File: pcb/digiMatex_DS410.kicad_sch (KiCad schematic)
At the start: 37 parts, among them J1 POWER, J2 E, J3 A/B, J4 Buttons, Q1 PN2222A, Q2 PN2222A, Q3 PN2222A, U1 MAX7219, U2 L7805

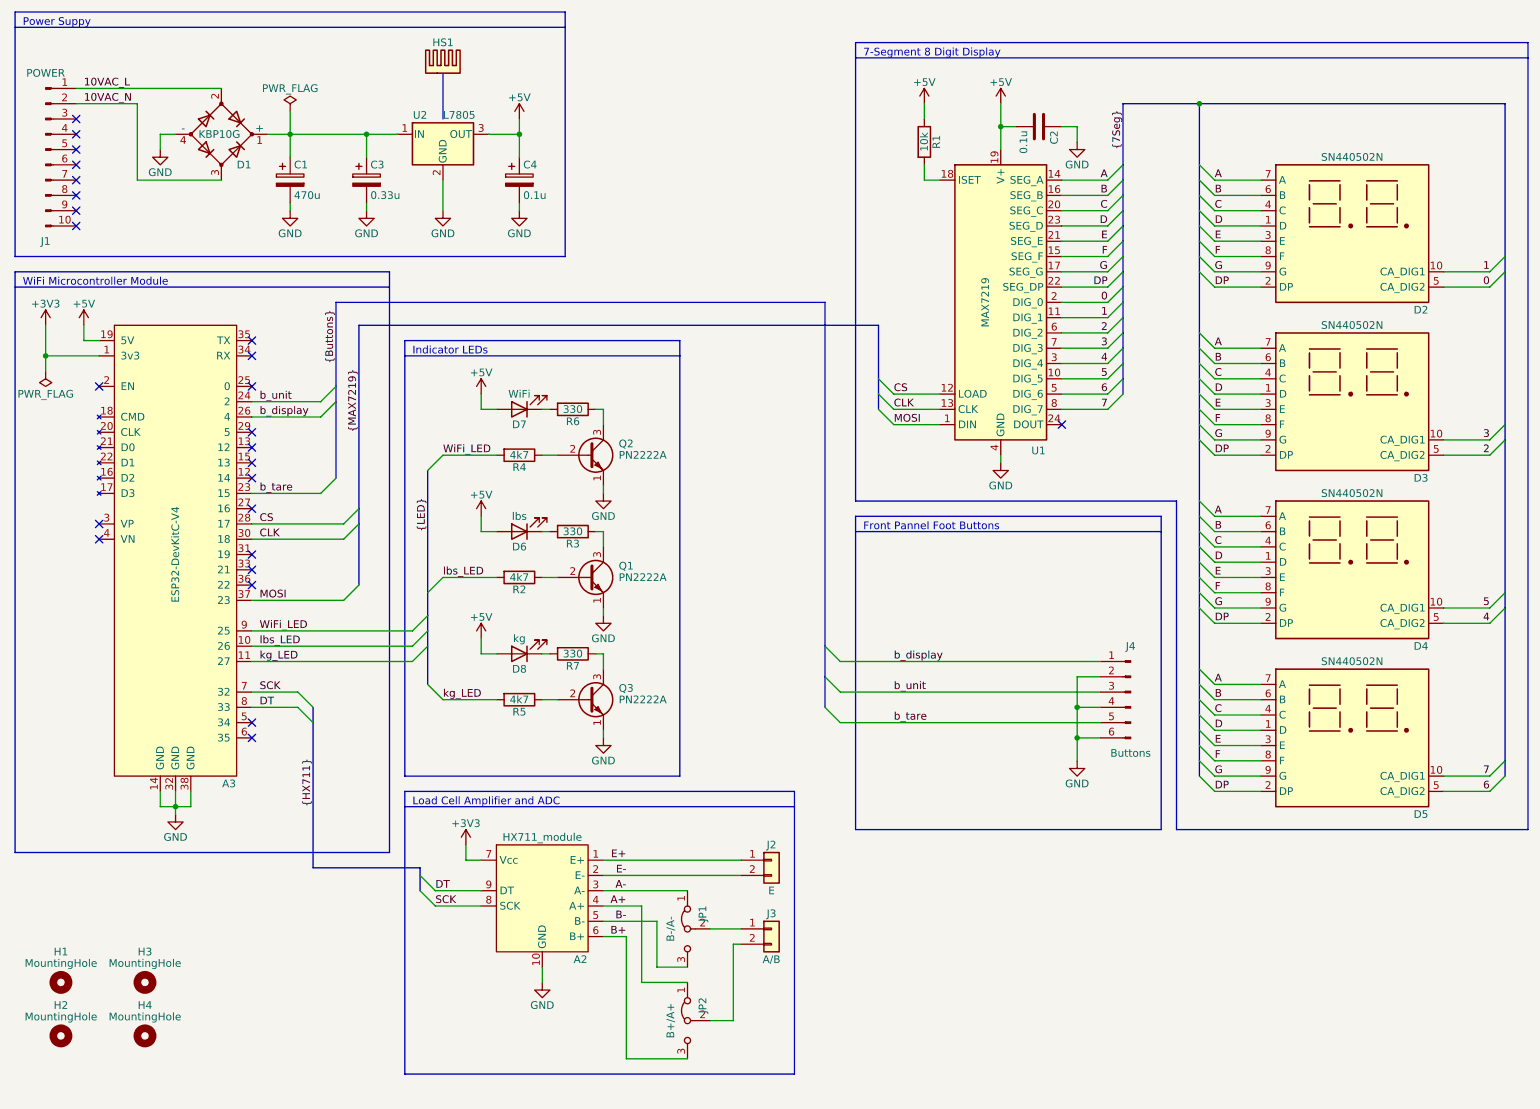
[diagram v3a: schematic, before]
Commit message: rev A schematic with more SMD
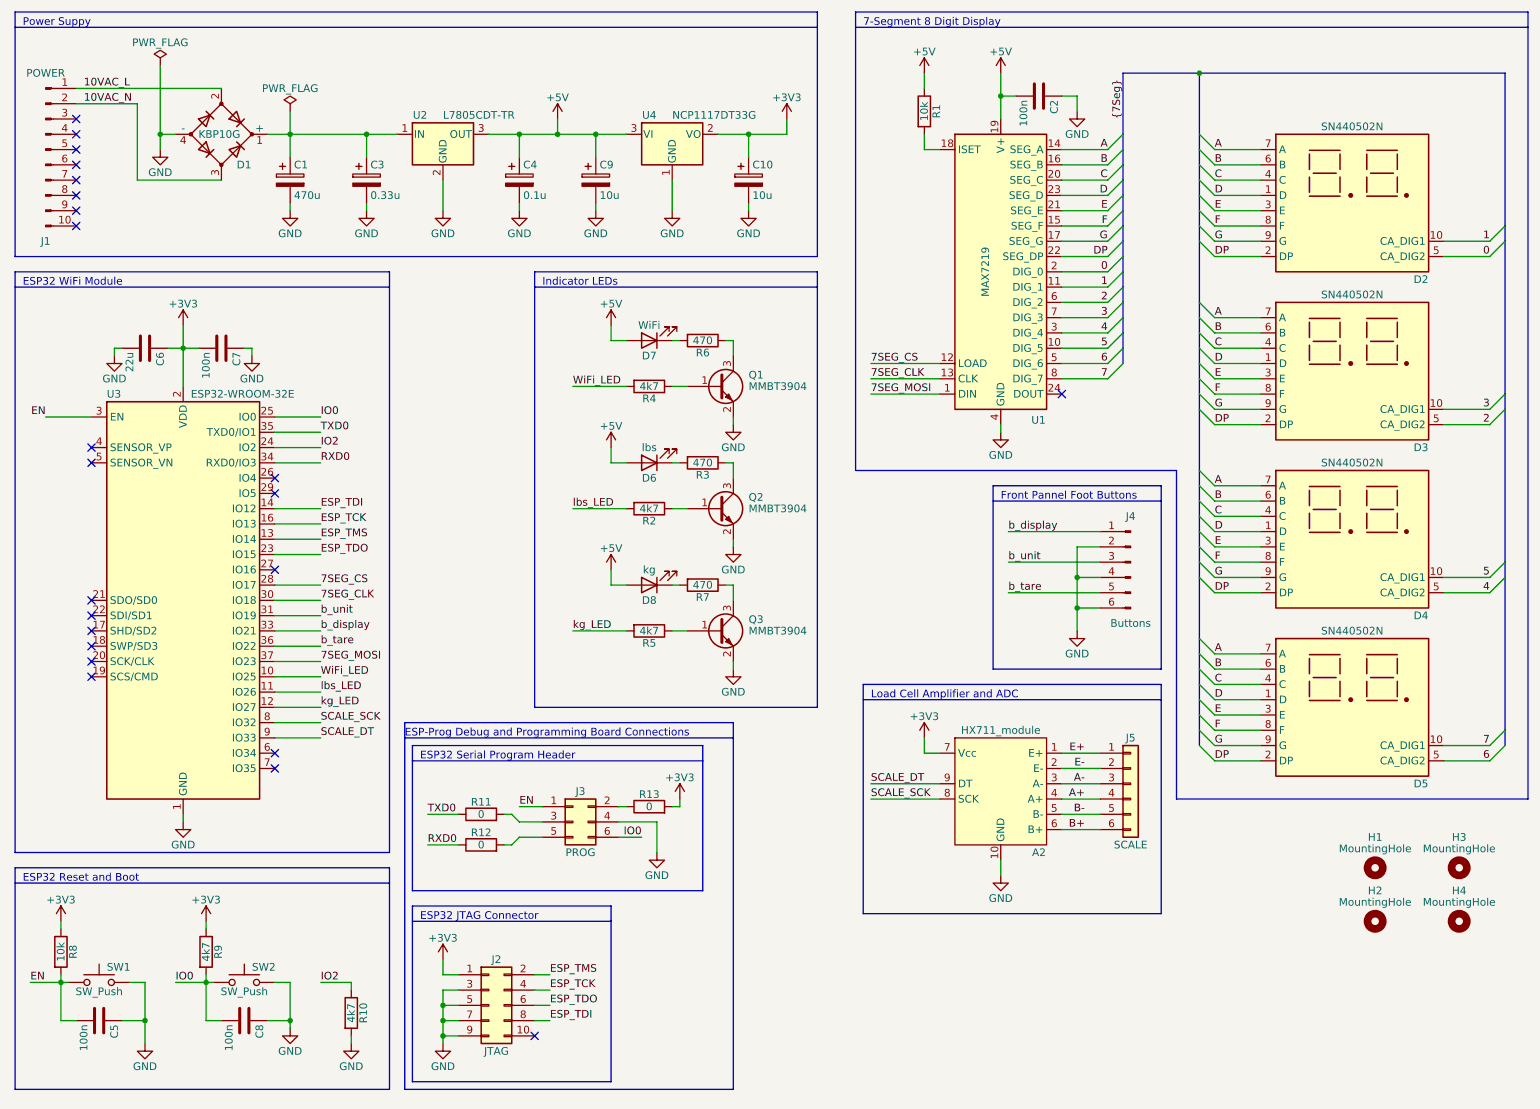
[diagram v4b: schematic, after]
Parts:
- removed A3: ESP32-DevKitC-V4, pl_esp:esp32_devkitc_v4, symbol pl_esp32:ESP32-DevKitC-V4
- removed HS1: Heatsink, pl_heatsink:TO-220hs_16x16x25mm_2pins, symbol Mechanical:Heatsink
- removed J2: E, pl_TerminalBlock:WJ127-5.0-2P, symbol Connector_Generic:Conn_01x02
- removed J3: A/B, pl_TerminalBlock:WJ127-5.0-2P, symbol Connector_Generic:Conn_01x02
- removed JP1: B-/A-, Connector_PinHeader_2.54mm:PinHeader_1x03_P2.54mm_Vertical, symbol Jumper:Jumper_3_Bridged12
- removed JP2: B+/A+, Connector_PinHeader_2.54mm:PinHeader_1x03_P2.54mm_Vertical, symbol Jumper:Jumper_3_Bridged12
- removed Q1, Q2, Q3: PN2222A, Package_TO_SOT_THT:TO-92_Inline, symbol Transistor_BJT:PN2222A
- added C10, C9: 10u, Capacitor_THT:CP_Radial_D6.3mm_P2.50mm, symbol Device:C_Polarized
- added C5, C7, C8: 100n, Capacitor_SMD:C_0603_1608Metric, symbol Device:C
- added C6: 22u, Capacitor_SMD:C_1206_3216Metric, symbol Device:C
- added J2: JTAG, Connector_PinHeader_2.54mm:PinHeader_2x05_P2.54mm_Vertical, symbol Connector_Generic:Conn_02x05_Odd_Even
- added J3: PROG, Connector_PinHeader_2.54mm:PinHeader_2x03_P2.54mm_Vertical, symbol Connector_Generic:Conn_02x03_Odd_Even
- added J5: SCALE, TerminalBlock_Phoenix:TerminalBlock_Phoenix_MKDS-1,5-6_1x06_P5.00mm_Horizontal, symbol Connector_Generic:Conn_01x06
- added Q1, Q2, Q3: MMBT3904, Package_TO_SOT_SMD:SOT-23, symbol Transistor_BJT:MMBT3904
- added R10, R9: 4k7, Capacitor_SMD:C_0603_1608Metric, symbol Device:R
- added R11, R12, R13: 0, Capacitor_SMD:C_0805_2012Metric, symbol Device:R
- added R8: 10k, Capacitor_SMD:C_0603_1608Metric, symbol Device:R
- added SW1, SW2: SW_Push, Button_Switch_THT:SW_PUSH_6mm, symbol Switch:SW_Push
- added U3: ESP32-WROOM-32E, RF_Module:ESP32-WROOM-32, symbol RF_Module:ESP32-WROOM-32D
- added U4: NCP1117DT33G, Package_TO_SOT_SMD:TO-252-2, symbol Regulator_Linear:NCP1117-3.3_TO252
- C2: value 0.1u -> 100n; footprint Capacitor_THT:C_Disc_D4.3mm_W1.9mm_P5.00mm -> Capacitor_SMD:C_0603_1608Metric
- R1, R2, R4, R5: footprint Resistor_THT:R_Axial_DIN0207_L6.3mm_D2.5mm_P15.24mm_Horizontal -> Capacitor_SMD:C_0603_1608Metric
- R3, R6, R7: value 330 -> 470; footprint Resistor_THT:R_Axial_DIN0207_L6.3mm_D2.5mm_P15.24mm_Horizontal -> Capacitor_SMD:C_0805_2012Metric
- U2: value L7805 -> L7805CDT-TR; footprint Package_TO_SOT_THT:TO-220-3_Vertical -> Package_TO_SOT_SMD:TO-252-2
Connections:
- net +3V3: now also C10.1, C6.1, C7.2, J2.1 (Pin_1), R13.2, R8.1, R9.1, U3.2 (VDD), U4.2 (VO)
- net +5V: now also C9.1, U4.3 (VI)
- net A+: now also J5.4 (Pin_4)
- net A-: now also J5.3 (Pin_3)
- net B+: now also J5.6 (Pin_6)
- net B-: now also J5.5 (Pin_5)
- net E+: now also J5.1 (Pin_1)
- net E-: now also J5.2 (Pin_2)
- net GND: now also C10.2, C5.1, C6.2, C7.1, C8.1, C9.2, J2.3 (Pin_3), J2.5 (Pin_5), J2.7 (Pin_7), J2.9 (Pin_9), J3.4 (Pin_4), Q1.2 (E), Q2.2 (E), Q3.2 (E), R10.2, SW1.2, SW2.2, U3.1 (GND), U3.15 (GND), U3.38 (GND), U3.39 (GND), U4.1 (GND)
- net WiFi_LED: now also U3.10 (IO25)
- net b_display: now also U3.33 (IO21)
- net b_tare: now also U3.36 (IO22)
- net b_unit: now also U3.31 (IO19)
- net kg_LED: now also U3.12 (IO27)
- net lbs_LED: now also U3.11 (IO26)
- net at R7.1: now also Q3.3 (C)
- net at R5.1: now also Q3.1 (B)
- net at R2.1: now also Q2.1 (B)
- net at R3.1: now also Q2.3 (C)
- net at R4.1: now also Q1.1 (B)
- net at R6.1: now also Q1.3 (C)
- net CLK renamed 7SEG_CLK
- net 7SEG_CLK: now also U3.30 (IO18)
- net CS renamed 7SEG_CS
- net 7SEG_CS: now also U3.28 (IO17)
- net DT renamed SCALE_DT
- net SCALE_DT: now also U3.9 (IO33)
- net MOSI renamed 7SEG_MOSI
- net 7SEG_MOSI: now also U3.37 (IO23)
- net SCK renamed SCALE_SCK
- net SCALE_SCK: now also U3.8 (IO32)
- new net: J3.2 (Pin_2), R13.1
- new net: J3.3 (Pin_3), R11.2
- new net: J3.5 (Pin_5), R12.2
- new net EN: C5.2, J3.1 (Pin_1), R8.2, SW1.1, U3.3 (EN)
- new net ESP_TCK: J2.4 (Pin_4), U3.16 (IO13)
- new net ESP_TDI: J2.8 (Pin_8), U3.14 (IO12)
- new net ESP_TDO: J2.6 (Pin_6), U3.23 (IO15)
- new net ESP_TMS: J2.2 (Pin_2), U3.13 (IO14)
- new net IO0: C8.2, J3.6 (Pin_6), R9.2, SW2.1, U3.25 (IO0)
- new net IO2: R10.1, U3.24 (IO2)
- new net RXD0: R12.1, U3.34 (RXD0/IO3)
- new net TXD0: R11.1, U3.35 (TXD0/IO1)
- no-connect marks 25 -> 23
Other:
- note added: "ESP-Prog Debug and Programming Board Connections"
- note added: "ESP32 JTAG Connector"
- note added: "ESP32 Reset and Boot"
- note added: "ESP32 Serial Program Header"
- note added: "ESP32 WiFi Module"
- note removed: "WiFi Microcontroller Module"
- moved on the sheet: A2, C2, D2, D3, D4, D5, D6, D7, D8, H1, H2, H3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

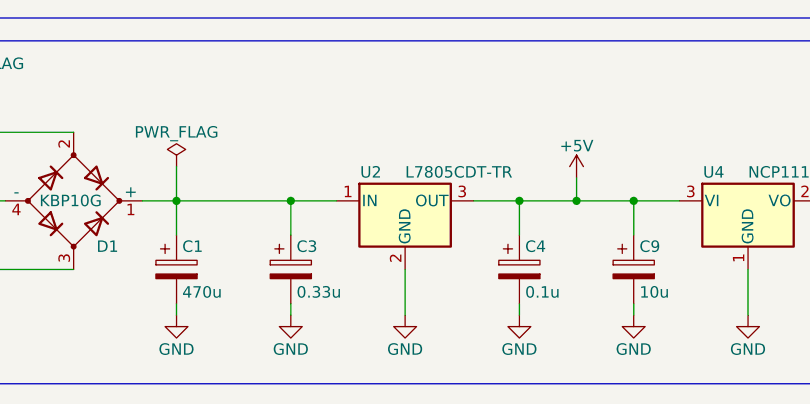
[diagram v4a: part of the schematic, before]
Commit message: Update digiMatex_DS410.kicad_sch
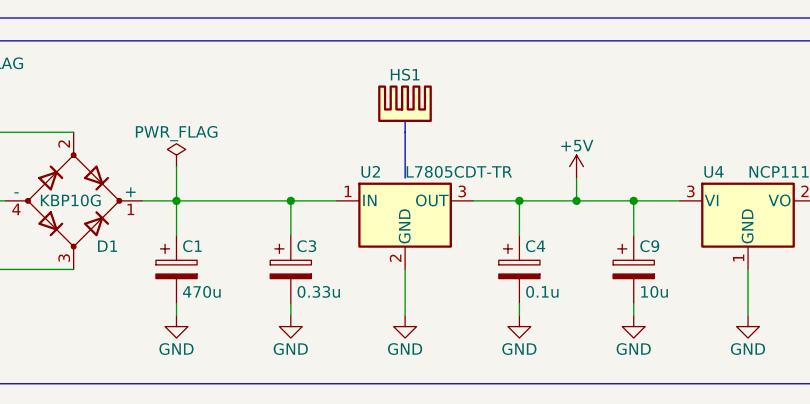
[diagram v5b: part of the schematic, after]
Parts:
- added HS1: Heatsink, pl_heatsink:TO-220hs_16x16x25mm_2pins, symbol Mechanical:Heatsink
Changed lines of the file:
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@@
     (comment 1 "PCB to be maufactured by prototype board house (JLCPCB)")
   )
-  (bus_alias "7Seg" (members "A" "B" "C" "D" "E" "F" "G" "DP" "1" "2" "3" "4" "5" "6" "7" "0"))
-  (bus_alias "LED" (members "WiFi_LED" "lbs_LED" "kg_LED"))
-  (bus_alias "MAX7219" (members "CLK" "MOSI" "CS"))
   (bus_alias "Buttons" (members "b_display" "b_tare" "b_unit"))
   (bus_alias "HX711" (members "SCK" "DT"))
+  (bus_alias "MAX7219" (members "CLK" "MOSI" "CS"))
+  (bus_alias "LED" (members "WiFi_LED" "lbs_LED" "kg_LED"))
+  (bus_alias "7Seg" (members "A" "B" "C" "D" "E" "F" "G" "DP" "1" "2" "3" "4" "5" "6" "7" "0"))
   (junction (at 110.49 34.29) (diameter 0) (color 0 0 0 0)
   )
@@
     (stroke (width 0) (type default) (color 0 0 0 0))
   )
+  (polyline (pts (xy 85.09 25.4) (xy 85.09 26.67))
+    (stroke (width 0) (type default) (color 0 0 0 0))
+  )
   (wire (pts (xy 213.36 67.31) (xy 220.98 67.31))
     (stroke (width 0) (type default) (color 0 0 0 0))
@@
     (stroke (width 0) (type default) (color 0 0 0 0))
   )
+  (polyline (pts (xy 85.09 26.67) (xy 85.09 31.75))
+    (stroke (width 0) (type default) (color 0 0 0 0))
+  )
   (polyline (pts (xy 204.47 163.83) (xy 154.94 163.83))
     (stroke (width 0) (type default) (color 0 0 0 0))
@@
     (pin "1")
   )
+  (symbol (lib_id "Mechanical:Heatsink") (at 85.09 25.4 0) (unit 1)
+    (in_bom yes) (on_board yes)
+    (property "Reference" "HS1" (id 0) (at 85.09 20.32 0))
+    (property "Value" "Heatsink" (id 1) (at 85.09 26.67 0)
+      (effects (font (size 1.27 1.27)) hide)
+    )
+    (property "Footprint" "pl_heatsink:TO-220hs_16x16x25mm_2pins" (id 2) (at 85.3948 25.4 0)
+      (effects (font (size 1.27 1.27)) hide)
+    )
+    (property "Datasheet" "~" (id 3) (at 85.3948 25.4 0)
+      (effects (font (size 1.27 1.27)) hide)
+    )
+  )
   (symbol (lib_id "Device:R") (at 119.38 146.05 90) (unit 1)
     (in_bom yes) (on_board yes)
@@
       (reference "H4") (unit 1) (value "MountingHole") (footprint "MountingHole:MountingHole_4mm_Pad")
     )
+    (path "/fbb7b3f5-b61c-4411-a813-3930d80b07fc"
+      (reference "HS1") (unit 1) (value "Heatsink") (footprint "pl_heatsink:TO-220hs_16x16x25mm_2pins")
+    )
     (path "/34c53cff-c073-4b59-a48d-10c7e18a985b"
